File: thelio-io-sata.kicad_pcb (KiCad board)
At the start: 2 copper layers, 80.2 x 71.8 mm, 6 parts

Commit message: Update SATA design
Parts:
- added REF**: MountingHole_3.2mm_M3, MountingHole:MountingHole_3.2mm_M3, F.Cu at (116.6, 73.9)
- added REF**: MountingHole_3.2mm_M3, MountingHole:MountingHole_3.2mm_M3, F.Cu at (48.6, 73.9)
- added REF**: MountingHole_3.2mm_M3, MountingHole:MountingHole_3.2mm_M3, F.Cu at (48.6, 52.9)
- added REF**: MountingHole_3.2mm_M3, MountingHole:MountingHole_3.2mm_M3, F.Cu at (116.6, 52.9)
- added REF**: MountingHole_3.2mm_M3, MountingHole:MountingHole_3.2mm_M3, F.Cu at (48.6, 31.9)
- added REF**: MountingHole_3.2mm_M3, MountingHole:MountingHole_3.2mm_M3, F.Cu at (116.6, 31.9)
- DATA0, DATA1, G***, POWER0: moved to F.Cu
- SATA0, SATA1: moved to B.Cu
- moved DATA0 30.1 mm to (90.3, 44.2), turned to 0 degrees
- moved DATA1 29.1 mm to (90.3, 54.2), turned to 0 degrees
- moved POWER0 18.0 mm to (66.7, 53.3), turned to 0 degrees
- moved SATA0 12.9 mm to (77.5, 31.2), turned to 180 degrees
- moved SATA1 12.1 mm to (77.5, 71.2), turned to 180 degrees
- moved G*** 7.71 mm to (80.6, 39.4), turned to 0 degrees
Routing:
- net +5V: track 40.7 -> 0.00 mm
- net +12V: track 40.0 -> 0.00 mm
- net GND: track 59.8 -> 21.0 mm, vias 18 -> 6
- net Net-(DATA0-Pad3): track 4.89 -> 15.6 mm
- net Net-(DATA0-Pad6): track 4.89 -> 15.6 mm
- net Net-(DATA0-Pad5): track 4.89 -> 15.6 mm
- net Net-(DATA0-Pad2): track 4.89 -> 15.6 mm
- net Net-(DATA1-Pad3): track 4.89 -> 14.5 mm
- net Net-(DATA1-Pad6): track 4.89 -> 14.5 mm
- net Net-(DATA1-Pad5): track 4.89 -> 14.5 mm
- net Net-(DATA1-Pad2): track 4.89 -> 14.5 mm
- added copper zone on B.Cu, net +12V
- added copper zone on B.Cu, net +5V
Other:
- board size 80.2 x 71.8 mm -> 74 x 50 mm
- board text added: "thelio-io-sata_1.0"

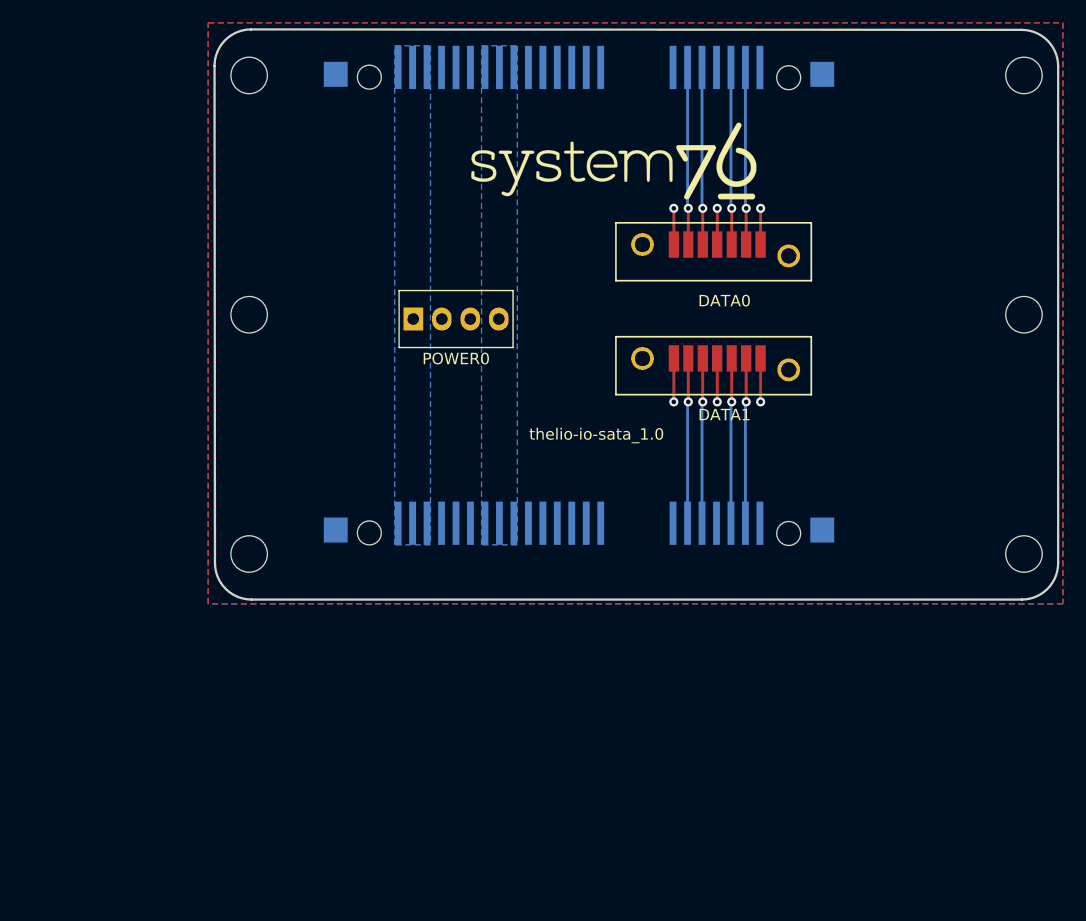
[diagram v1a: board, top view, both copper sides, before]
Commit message: signal integrity on SATA lines Add stackup with controlled impedance, 4 layers ground planes on inners ground vias plane cutouts
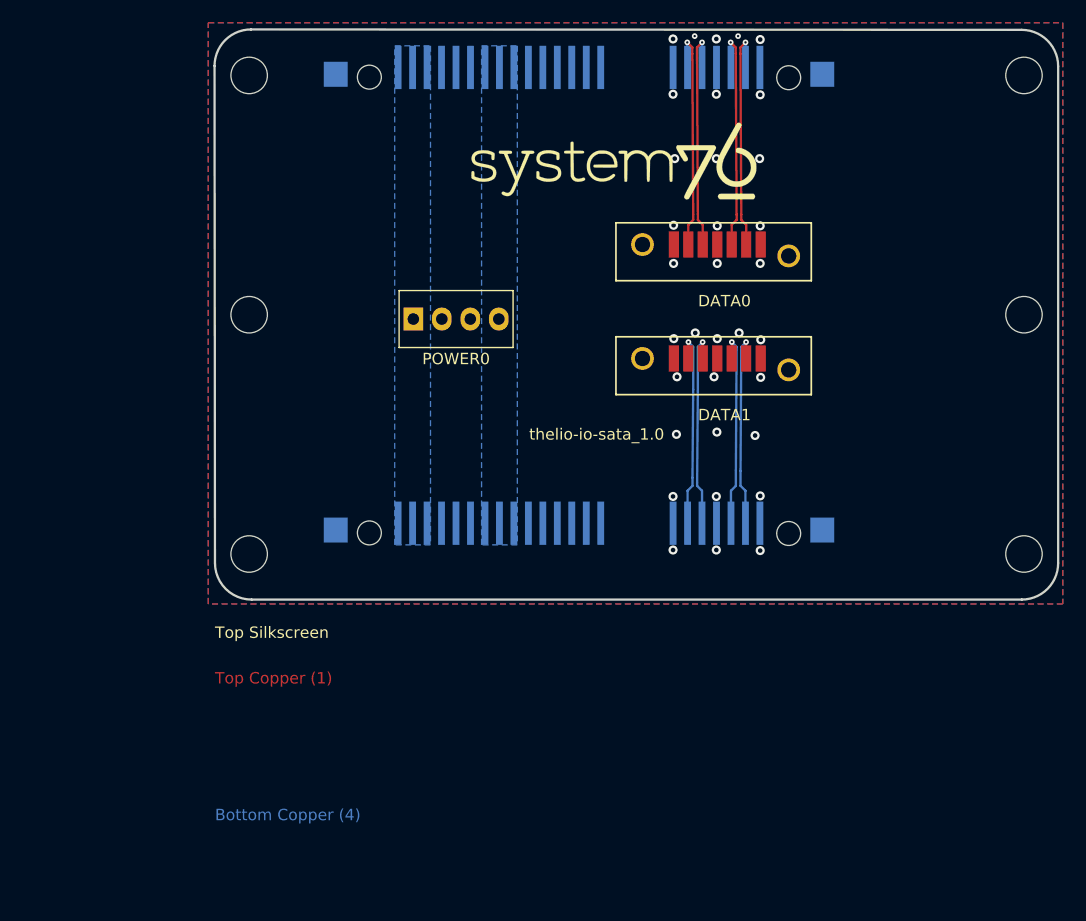
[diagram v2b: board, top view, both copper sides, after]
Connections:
- DATA0 pad 2: Net-(DATA0-Pad2) -> /SATA0_A+
- DATA0 pad 3: Net-(DATA0-Pad3) -> /SATA0_A-
- DATA0 pad 5: Net-(DATA0-Pad5) -> /SATA0_B-
- DATA0 pad 6: Net-(DATA0-Pad6) -> /SATA0_B+
- DATA1 pad 2: Net-(DATA1-Pad2) -> /SATA1_A+
- DATA1 pad 3: Net-(DATA1-Pad3) -> /SATA1_A-
- DATA1 pad 5: Net-(DATA1-Pad5) -> /SATA1_B-
- DATA1 pad 6: Net-(DATA1-Pad6) -> /SATA1_B+
- SATA0 pad 2: Net-(DATA0-Pad6) -> /SATA0_A+
- SATA0 pad 3: Net-(DATA0-Pad5) -> /SATA0_A-
- SATA0 pad 5: Net-(DATA0-Pad3) -> /SATA0_B-
- SATA0 pad 6: Net-(DATA0-Pad2) -> /SATA0_B+
- SATA1 pad 2: Net-(DATA1-Pad6) -> /SATA1_A+
- SATA1 pad 3: Net-(DATA1-Pad5) -> /SATA1_A-
- SATA1 pad 5: Net-(DATA1-Pad3) -> /SATA1_B-
- SATA1 pad 6: Net-(DATA1-Pad2) -> /SATA1_B+
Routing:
- net /SATA0_B+: track 0.00 -> 20.3 mm, vias 0 -> 1
- net /SATA0_A-: track 0.00 -> 20.3 mm, vias 0 -> 1
- net /SATA0_B-: track 0.00 -> 20.3 mm, vias 0 -> 1
- net /SATA0_A+: track 0.00 -> 20.3 mm, vias 0 -> 1
- net GND: track 21.0 -> 2.55 mm, vias 6 -> 34
- net /SATA1_B+: track 0.00 -> 17.7 mm, vias 0 -> 1
- net /SATA1_B-: track 0.00 -> 17.7 mm, vias 0 -> 1
- net /SATA1_A+: track 0.00 -> 17.7 mm, vias 0 -> 1
- net /SATA1_A-: track 0.00 -> 17.7 mm, vias 0 -> 1
- net Net-(DATA0-Pad3): track 15.6 -> 0.00 mm, vias 1 -> 0
- net Net-(DATA0-Pad6): track 15.6 -> 0.00 mm, vias 1 -> 0
- net Net-(DATA0-Pad5): track 15.6 -> 0.00 mm, vias 1 -> 0
- net Net-(DATA0-Pad2): track 15.6 -> 0.00 mm, vias 1 -> 0
- net Net-(DATA1-Pad3): track 14.5 -> 0.00 mm, vias 1 -> 0
- net Net-(DATA1-Pad6): track 14.5 -> 0.00 mm, vias 1 -> 0
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- added copper zone on In1.Cu, net GND
- added copper zone on In2.Cu, net GND
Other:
- copper layers 2 -> 4
- board text added: "Bottom Copper (4)"
- board text added: "Bottom Silkscreen"
- board text added: "Bottom Soldermask"
- board text added: "Controlled impedance: Layer 1 ref layer 2, 100 +- 10% ohm diff: 0.205 mm trace, 0.2032 mm space Layer 4 ref layer 3, 100 +- 10% ohm diff: 0.205 mm trace, 0.2032 mm space"
- board text added: "Core: 1.3 mm typical"
- board text added: "Inner Copper (2)"
- board text added: "Inner Copper (3)"
- board text added: "Prepreg: 7628 or as required for controlled impedance"
- board text added: "Top Copper (1)"
- board text added: "Top Silkscreen"
- board text added: "Top Soldermask"
- board text added: "thelio-io-sata_1.0 Board must be RoHS compliant Fabricate to IPC-A-600 Class II Material: Shengyi S1000-2 or equivalent Inner copper 1 or 1/2 oz Outer copper, min 33.4 um finished Black LPI solder mask over bare copper Vendor may remove solder mask from via holes, maximum of drill size + 3 mil Finish: OSP Silkscreen: white non conductive 100% electrical test required Remove all unused pads from i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"

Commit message: correct core thickness turn off high contrast
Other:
- board text added: "Core: as required for overall thickness"
- board text removed: "Core: 1.3 mm typical"
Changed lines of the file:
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@@
     (effects (font (size 1 1) (thickness 0.15)) (justify left))
   )
-  (gr_text "Core: 1.3 mm typical" (at 52.566562 90.82) (layer "Cmts.User")
+  (gr_text "Core: as required for overall thickness" (at 52.566562 90.82) (layer "Cmts.User")
     (effects (font (size 1 1) (thickness 0.15)) (justify left))
   )

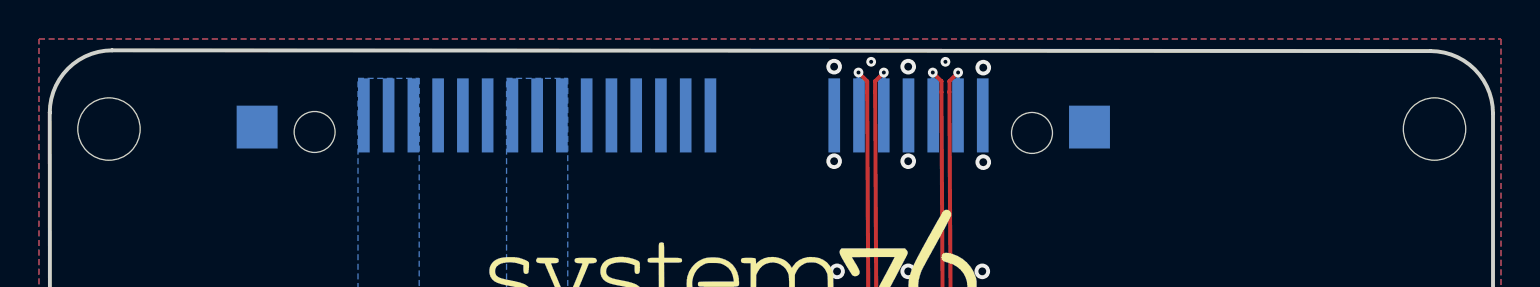
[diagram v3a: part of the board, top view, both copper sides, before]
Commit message: Fix top edge of thelio-io-sata
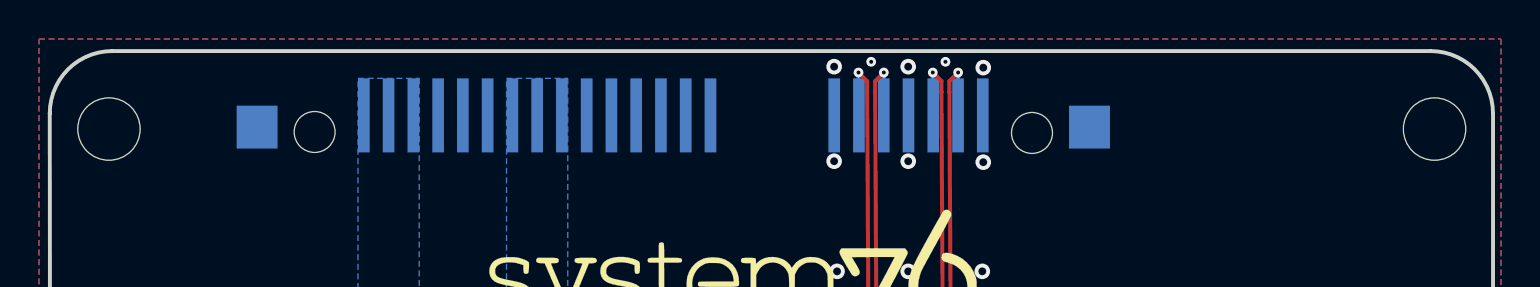
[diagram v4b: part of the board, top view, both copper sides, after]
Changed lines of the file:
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@@
     )
   )
-  (gr_line (start 48.729304 27.882742) (end 116.366562 27.92) (layer "Edge.Cuts") (width 0.2))
+  (gr_line (start 48.729304 27.92) (end 116.366562 27.92) (layer "Edge.Cuts") (width 0.2))
   (gr_line (start 116.366562 77.92) (end 48.776562 77.92) (layer "Edge.Cuts") (width 0.2))
   (gr_line (start 45.566562 74.72) (end 45.529304 31.082742) (layer "Edge.Cuts") (width 0.2))
-  (gr_arc (start 45.529304 31.082742) (mid 46.466562 28.82) (end 48.729304 27.882742) (layer "Edge.Cuts") (width 0.2))
+  (gr_arc (start 45.529304 31.12) (mid 46.466562 28.857258) (end 48.729304 27.92) (layer "Edge.Cuts") (width 0.2))
   (gr_arc (start 116.366562 27.92) (mid 118.629304 28.857258) (end 119.566562 31.12) (layer "Edge.Cuts") (width 0.2))
   (gr_arc (start 48.776562 77.92) (mid 46.510281 76.983347) (end 45.566562 74.72) (layer "Edge.Cuts") (width 0.2))
@@
     (connect_pads (clearance 0))
     (min_thickness 0.2)
-    (keepout (tracks allowed) (vias allowed) (pads allowed) (copperpour not_allowed) (footprints allowed))
+    (keepout (tracks allowed) (vias allowed) (pads allowed ) (copperpour not_allowed) (footprints allowed))
     (fill (thermal_gap 0.508) (thermal_bridge_width 0.508))
     (polygon
@@
     (connect_pads (clearance 0))
     (min_thickness 0.2)
-    (keepout (tracks allowed) (vias allowed) (pads allowed) (copperpour not_allowed) (footprints allowed))
+    (keepout (tracks allowed) (vias allowed) (pads allowed ) (copperpour not_allowed) (footprints allowed))
     (fill (thermal_gap 0.508) (thermal_bridge_width 0.508))
     (polygon
@@
     (connect_pads (clearance 0))
     (min_thickness 0.254)
-    (keepout (tracks allowed) (vias allowed) (pads allowed) (copperpour not_allowed) (footprints allowed))
+    (keepout (tracks allowed) (vias allowed) (pads allowed ) (copperpour not_allowed) (footprints allowed))
     (fill (thermal_gap 0.508) (thermal_bridge_width 0.508))
     (polygon
@@
     (connect_pads (clearance 0))
     (min_thickness 0.254)
-    (keepout (tracks allowed) (vias allowed) (pads allowed) (copperpour not_allowed) (footprints allowed))
+    (keepout (tracks allowed) (vias allowed) (pads allowed ) (copperpour not_allowed) (footprints allowed))
     (fill (thermal_gap 0.508) (thermal_bridge_width 0.508))
     (polygon
@@
     (connect_pads (clearance 0))
     (min_thickness 0.254)
-    (keepout (tracks allowed) (vias allowed) (pads allowed) (copperpour not_allowed) (footprints allowed))
+    (keepout (tracks allowed) (vias allowed) (pads allowed ) (copperpour not_allowed) (footprints allowed))
     (fill (thermal_gap 0.508) (thermal_bridge_width 0.508))
     (polygon
@@
     (connect_pads (clearance 0))
     (min_thickness 0.254)
-    (keepout (tracks allowed) (vias allowed) (pads allowed) (copperpour not_allowed) (footprints allowed))
+    (keepout (tracks allowed) (vias allowed) (pads allowed ) (copperpour not_allowed) (footprints allowed))
     (fill (thermal_gap 0.508) (thermal_bridge_width 0.508))
     (polygon
@@
     (connect_pads (clearance 0))
     (min_thickness 0.254)
-    (keepout (tracks allowed) (vias allowed) (pads allowed) (copperpour not_allowed) (footprints allowed))
+    (keepout (tracks allowed) (vias allowed) (pads allowed ) (copperpour not_allowed) (footprints allowed))
     (fill (thermal_gap 0.508) (thermal_bridge_width 0.508))
     (polygon
@@
     (connect_pads (clearance 0))
     (min_thickness 0.254)
-    (keepout (tracks allowed) (vias allowed) (pads allowed) (copperpour not_allowed) (footprints allowed))
+    (keepout (tracks allowed) (vias allowed) (pads allowed ) (copperpour not_allowed) (footprints allowed))
     (fill (thermal_gap 0.508) (thermal_bridge_width 0.508))
     (polygon
@@
     (connect_pads (clearance 0))
     (min_thickness 0.254)
-    (keepout (tracks allowed) (vias allowed) (pads allowed) (copperpour not_allowed) (footprints allowed))
+    (keepout (tracks allowed) (vias allowed) (pads allowed ) (copperpour not_allowed) (footprints allowed))
     (fill (thermal_gap 0.508) (thermal_bridge_width 0.508))
     (polygon
@@
     (connect_pads (clearance 0))
     (min_thickness 0.254)
-    (keepout (tracks allowed) (vias allowed) (pads allowed) (copperpour not_allowed) (footprints allowed))
+    (keepout (tracks allowed) (vias allowed) (pads allowed ) (copperpour not_allowed) (footprints allowed))
     (fill (thermal_gap 0.508) (thermal_bridge_width 0.508))
     (polygon
@@
     (connect_pads (clearance 0))
     (min_thickness 0.2)
-    (keepout (tracks allowed) (vias allowed) (pads allowed) (copperpour not_allowed) (footprints allowed))
+    (keepout (tracks allowed) (vias allowed) (pads allowed ) (copperpour not_allowed) (footprints allowed))
     (fill (thermal_gap 0.508) (thermal_bridge_width 0.508))
     (polygon
@@
     (connect_pads (clearance 0))
     (min_thickness 0.2)
-    (keepout (tracks allowed) (vias allowed) (pads allowed) (copperpour not_allowed) (footprints allowed))
-    (fill (thermal_gap 0.508) (thermal_bridge_width 0.508))
-    (polygon
+    (keepout (tracks allowed) (vias allowed) (pads allowed ) (copperpour not_allowed) (footprints allowed))
+    (fill (thermal_gap 0.508) (thermal_bridge_width 0.508))
+    (polygon
